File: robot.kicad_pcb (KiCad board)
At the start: 2 copper layers, 55.2 x 89.3 mm, 67 parts, among them J1 PCA9865 2, J10 BATT out, J2 I2S, J3 Programming, J4 IMU, J5 Switches, J6 Expansion, J7 VCC, J8 Servo pwr, J9 BATT in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

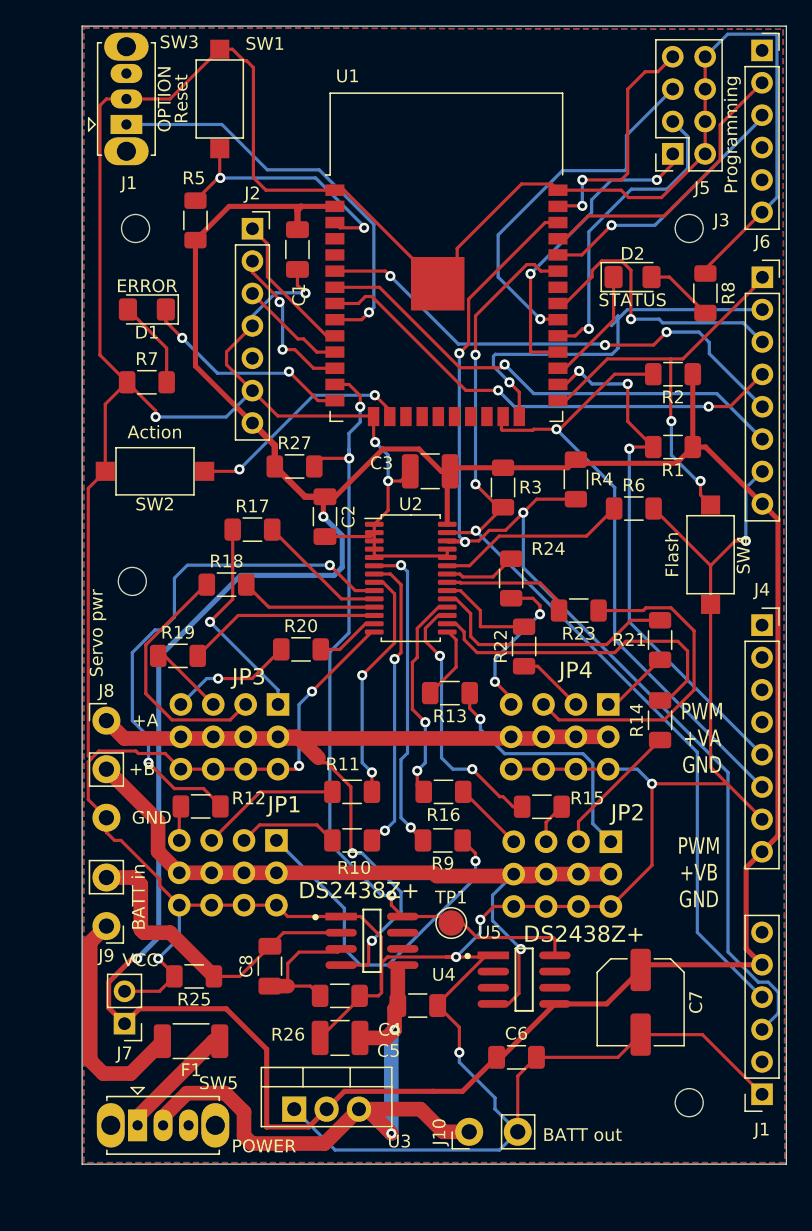
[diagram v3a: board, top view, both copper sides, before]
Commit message: Added minor footprint changes after trying to build the board. Added pin to switch battery to Vin.
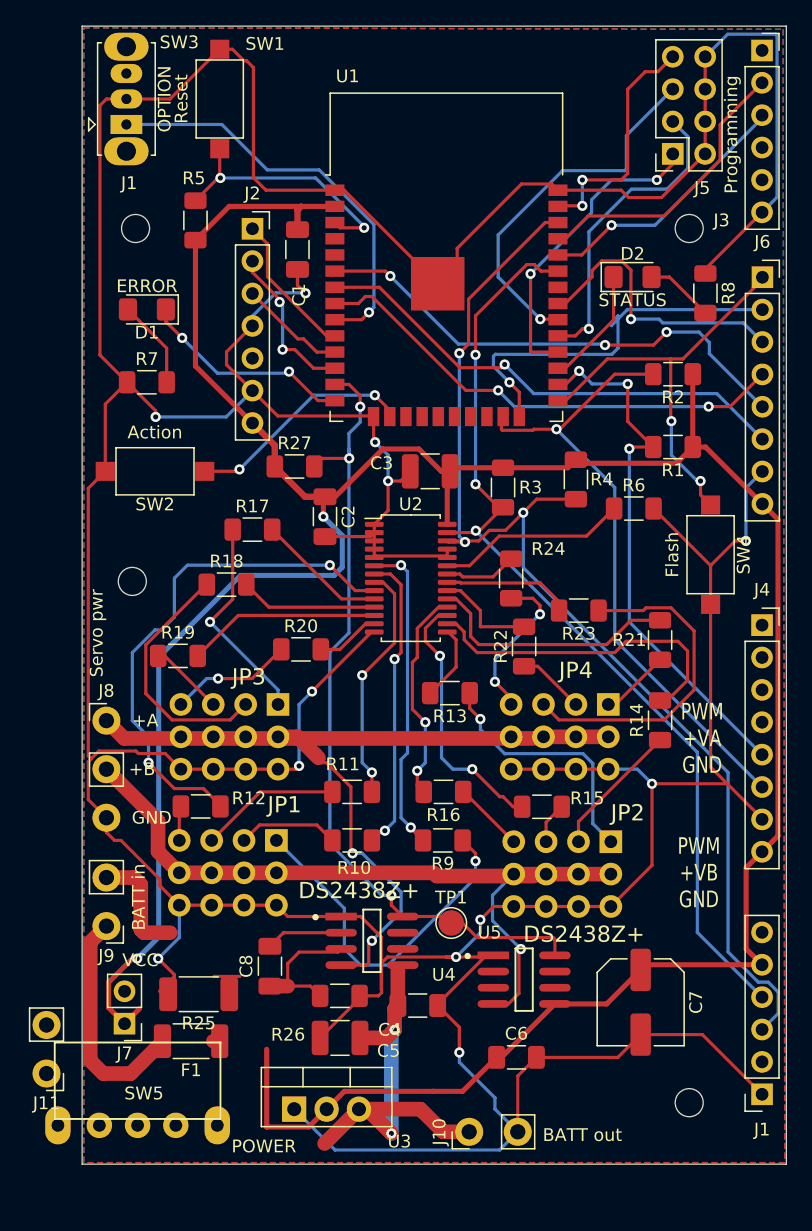
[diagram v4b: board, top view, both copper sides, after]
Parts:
- added J11: Vin, Connector_PinHeader_2.54mm:Connector_Battery_SolderPads, F.Cu at (93.1, 178.1)
- R25: footprint Resistor_SMD:R_1206_3216Metric_Pad1.30x1.75mm_HandSolder -> Resistor_SMD:R_2010_5025Metric_Pad1.40x2.65mm_HandSolder
- SW5: footprint Button_Switch_THT:SW_Slide_1P2T_CK_OS102011MS2Q -> KiCAD Custom Libs:Switch-SS12F23
- moved R25 1.44 mm to (105.0, 171.8)
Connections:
- SW5 pad 3: (no net) -> Net-(SW5-Pad3)
- U3 pad 1: GND -> +BATT
- U3 pad 2: VCC -> GND
- U3 pad 3: +BATT -> VCC
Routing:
- net +BATT: track 49.9 -> 33.1 mm
- net VCC: track 243.9 -> 232.6 mm
- net Net-(F1-Pad1): track 9.57 -> 0.50 mm
- net Net-(C8-Pad2): track 25.1 -> 16.9 mm
- net GND: track 454.2 -> 451.5 mm

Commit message: Added extra pins and input from revision 1.
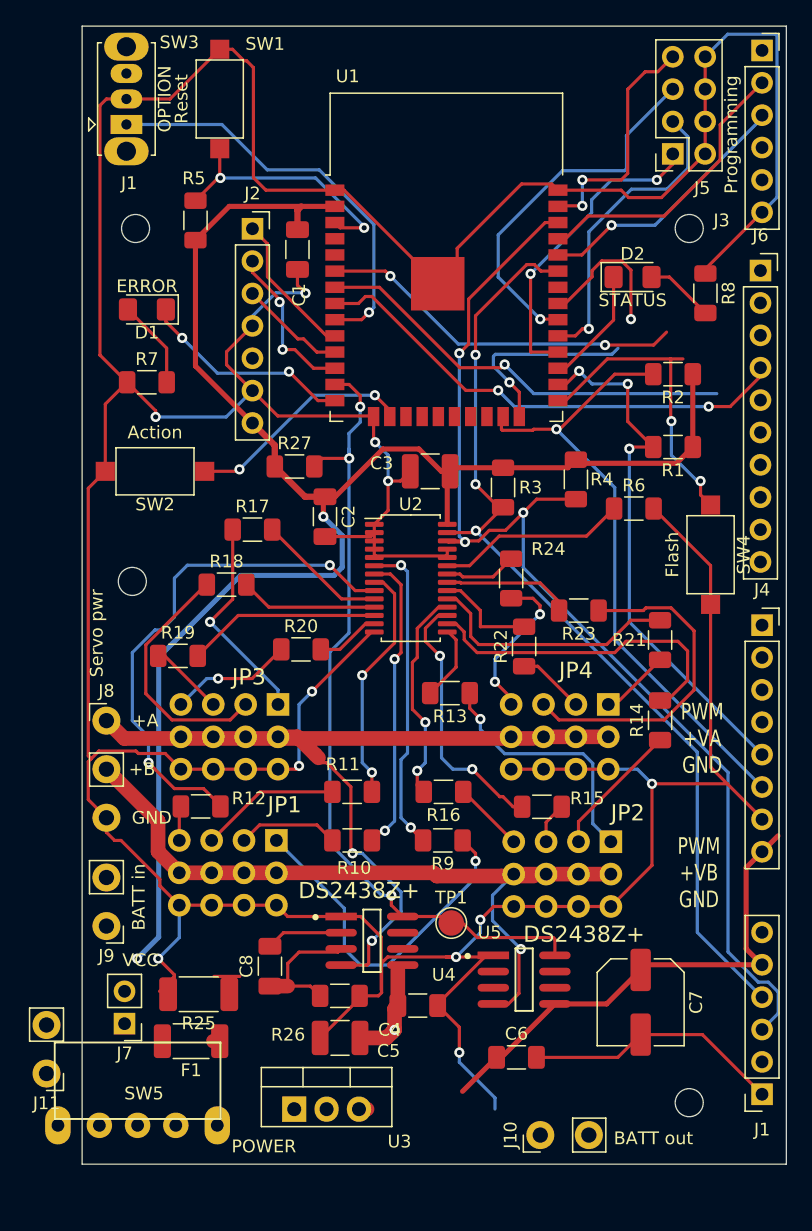
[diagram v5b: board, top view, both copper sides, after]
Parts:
- J6: footprint Connector_PinSocket_2.54mm:PinSocket_1x08_P2.54mm_Vertical -> Connector_PinSocket_2.54mm:PinSocket_1x10_P2.54mm_Vertical
- moved J10 5.58 mm to (131.8, 182.9)
- moved J6 0.54 mm to (149.1, 115.1)
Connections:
- J6 pad 7: GND -> /IO_36
- J6 pad 8: VCC -> /IO_39
- U1 pad 4: unconnected-(U1-Pad4) -> /IO_36
- U1 pad 5: unconnected-(U1-Pad5) -> /IO_39
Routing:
- net VCC: track 232.6 -> 168.3 mm
- net GND: track 451.5 -> 413.5 mm, vias 12 -> 11
- net +BATT: track 33.1 -> 8.68 mm, vias 2 -> 1
- net Net-(F1-Pad2): track 18.2 -> 0.05 mm
- net /IO_2: track 31.5 -> 15.6 mm
- net /IO_19: track 22.0 -> 11.0 mm
- net /IO_34: track 39.3 -> 28.8 mm, vias 3 -> 2
- net Net-(C8-Pad2): track 16.9 -> 8.06 mm
- net /IO_0: track 32.3 -> 23.5 mm
- net /IO_35: track 38.7 -> 33.6 mm
- removed copper zone on B.Cu, net GND
- removed copper zone on F.Cu, net GND
